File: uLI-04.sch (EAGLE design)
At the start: 40 parts, among them IC1 PIC18F14K50-I/SS, IC2 ADM2483, IC4 78L05F, J1 PICPROG2-V, J5 WEBP6-4, J6 WEBP6-4, J7 WEBP6-4, Q1 12.00 MHz, T1 IRF7306, X1 MINI-USB_SHIELD4P-USB-SPEC, X2 ARK1550/2_S

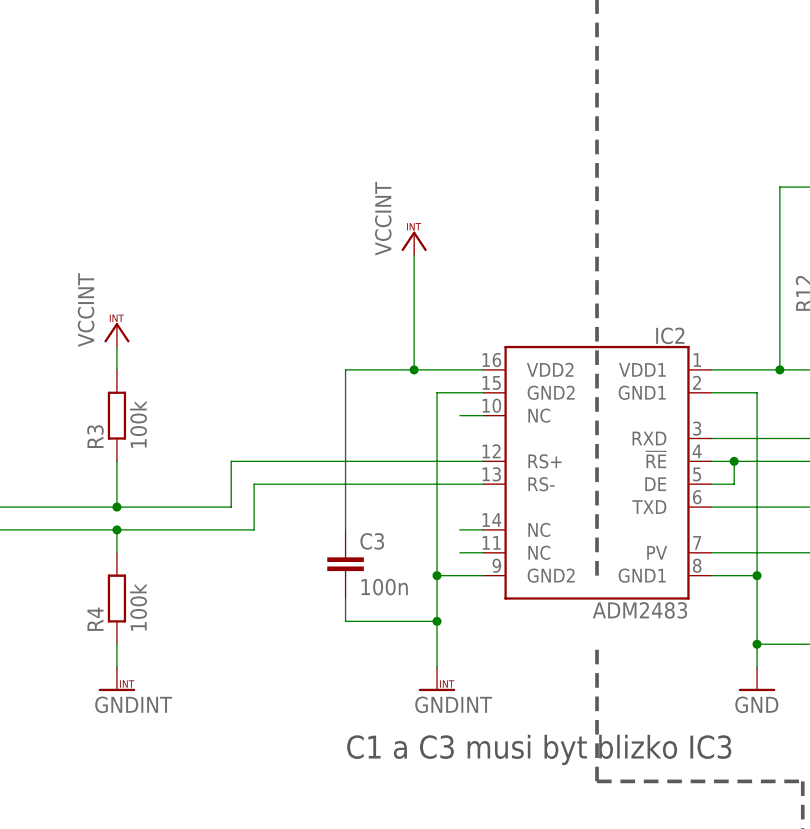
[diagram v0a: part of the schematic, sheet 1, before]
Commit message: Odstranen prebytecny kondenzator 100 n.
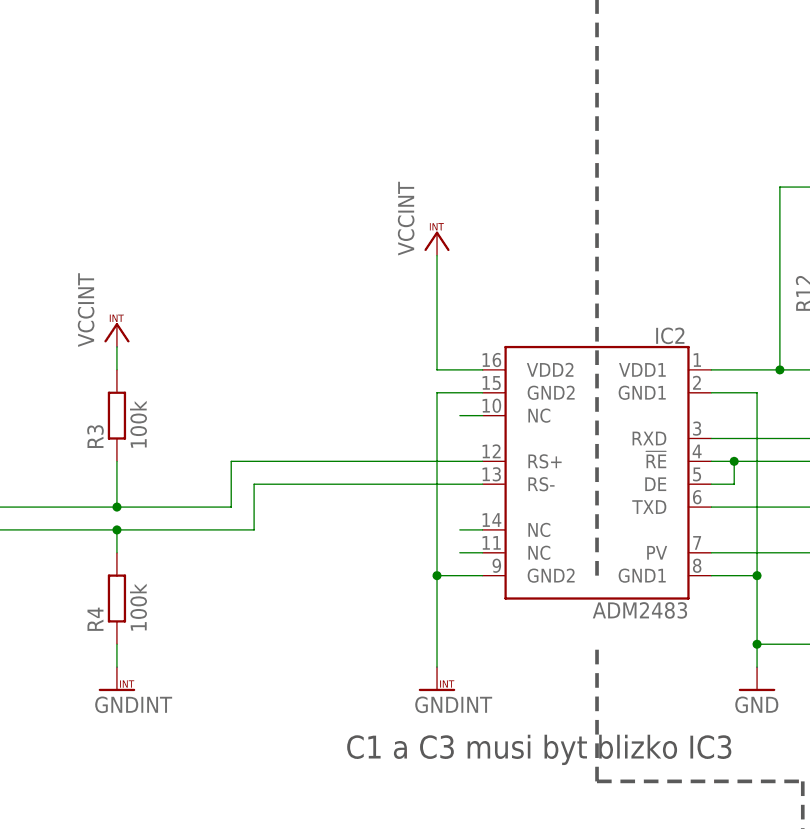
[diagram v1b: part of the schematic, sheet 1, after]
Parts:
- removed C3: 100n, rcl:C-EUC1206
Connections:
- net GNDINT: no longer C3.2
- net VCCINT: no longer C3.1
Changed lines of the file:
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@@
 </classes>
 <parts>
-<part name="C3" library="rcl" deviceset="C-EU" device="C1206" value="100n"/>
 <part name="U$1" library="frames" deviceset="FRAME_M1" device=""/>
 <part name="IC1" library="microchip" deviceset="PIC18*K50" device="-I/SS" technology="F14"/>
@@
 </plain>
 <instances>
-<instance part="C3" gate="G$1" x="91.44" y="76.2"/>
 <instance part="U$1" gate="G$1" x="0" y="0"/>
 <instance part="IC1" gate="A" x="195.58" y="91.44"/>
@@
 <instance part="GND3" gate="1" x="137.16" y="60.96"/>
 <instance part="GND4" gate="G$1" x="101.6" y="60.96"/>
-<instance part="VCC1" gate="G$1" x="99.06" y="111.76"/>
+<instance part="VCC1" gate="G$1" x="101.6" y="111.76"/>
 <instance part="C4" gate="G$1" x="147.32" y="76.2"/>
 <instance part="X1" gate="A" x="241.3" y="83.82"/>
@@
 <wire x1="101.6" y1="93.98" x2="101.6" y2="73.66" width="0.1524" layer="91"/>
 <wire x1="101.6" y1="73.66" x2="106.68" y2="73.66" width="0.1524" layer="91"/>
-<wire x1="101.6" y1="73.66" x2="101.6" y2="68.58" width="0.1524" layer="91"/>
 <junction x="101.6" y="73.66"/>
 <pinref part="GND4" gate="G$1" pin="GNDINT"/>
-<pinref part="C3" gate="G$1" pin="2"/>
-<wire x1="101.6" y1="68.58" x2="101.6" y2="63.5" width="0.1524" layer="91"/>
-<wire x1="101.6" y1="68.58" x2="91.44" y2="68.58" width="0.1524" layer="91"/>
-<wire x1="91.44" y1="68.58" x2="91.44" y2="71.12" width="0.1524" layer="91"/>
-<junction x="101.6" y="68.58"/>
+<wire x1="101.6" y1="73.66" x2="101.6" y2="63.5" width="0.1524" layer="91"/>
 <pinref part="IC2" gate="A" pin="GND2@2"/>
 <pinref part="IC2" gate="A" pin="GND2@1"/>
@@
 <net name="VCCINT" class="1">
 <segment>
-<wire x1="99.06" y1="96.52" x2="99.06" y2="109.22" width="0.1524" layer="91"/>
-<wire x1="106.68" y1="96.52" x2="99.06" y2="96.52" width="0.1524" layer="91"/>
-<junction x="99.06" y="96.52"/>
+<wire x1="101.6" y1="96.52" x2="101.6" y2="109.22" width="0.1524" layer="91"/>
+<wire x1="106.68" y1="96.52" x2="101.6" y2="96.52" width="0.1524" layer="91"/>
 <pinref part="VCC1" gate="G$1" pin="VCCINT"/>
-<pinref part="C3" gate="G$1" pin="1"/>
-<wire x1="91.44" y1="78.74" x2="91.44" y2="96.52" width="0.1524" layer="91"/>
-<wire x1="91.44" y1="96.52" x2="99.06" y2="96.52" width="0.1524" layer="91"/>
 <pinref part="IC2" gate="A" pin="VDD2"/>
 </segment>

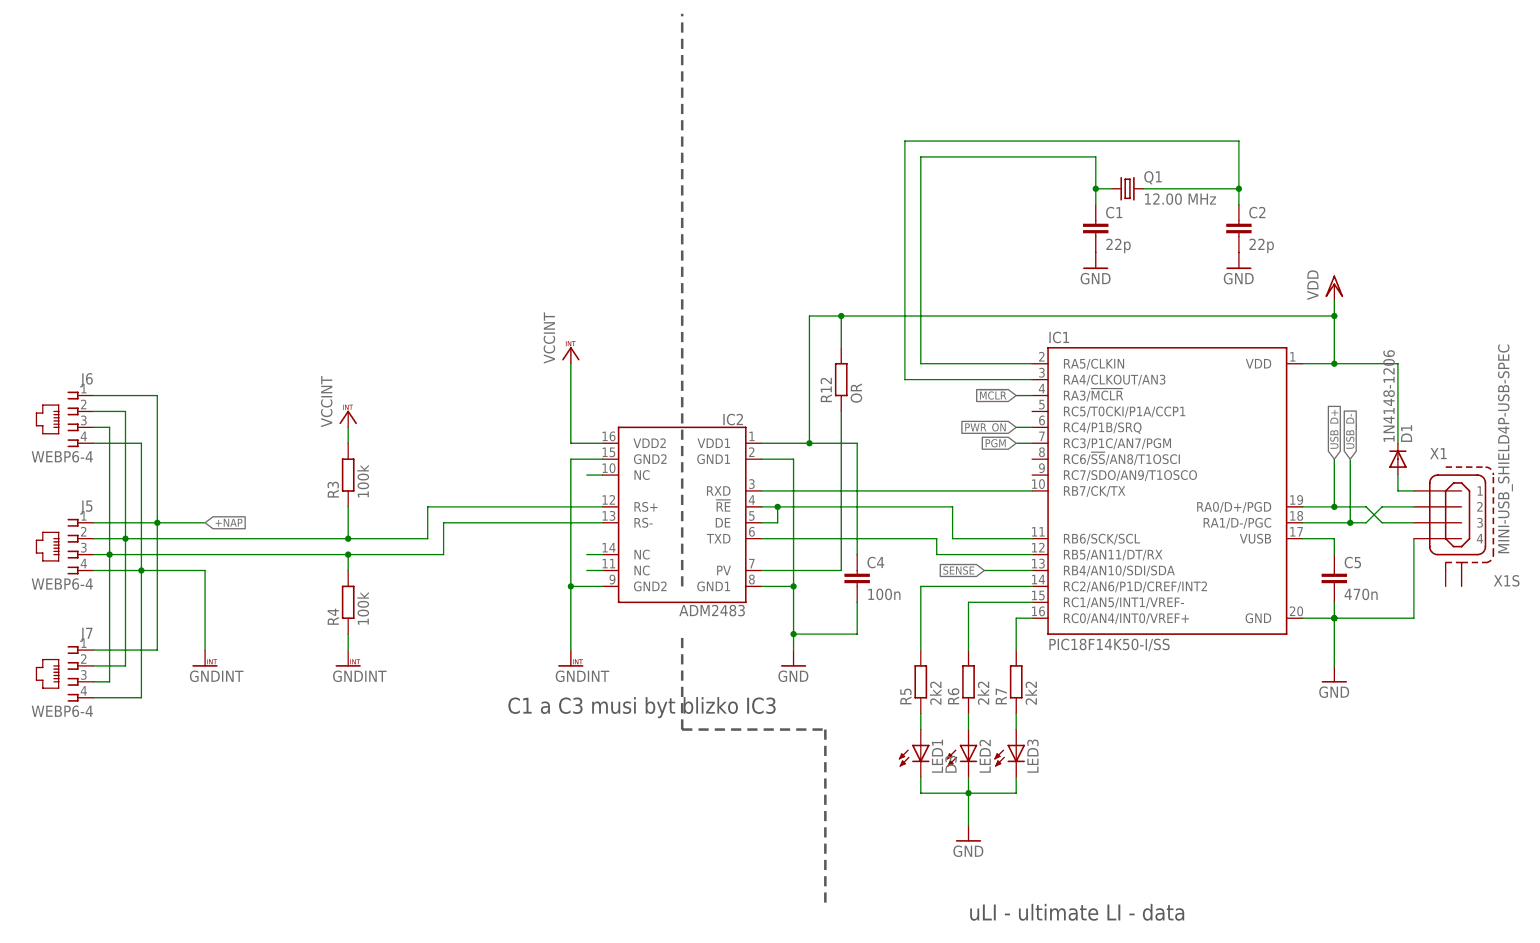
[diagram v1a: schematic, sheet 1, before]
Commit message: uLI-04 rev 2.
Opraveny chyby uLI-04 zjistene behem testovani:
 * upraven obrys krabicky podle realnych rozmeru (zvetseno symtetricky 1 mm do sirky a 0.5 mm do vysky)
 * posunuty otvory pro srouby do krabicky o 0.5 mm v kazde ose smerrem ke kraji
 * prohozeno RX a TX mezi procesorem a ADUMem
 * opraveno zdcadlove zapojeni XpressNETich konektoru
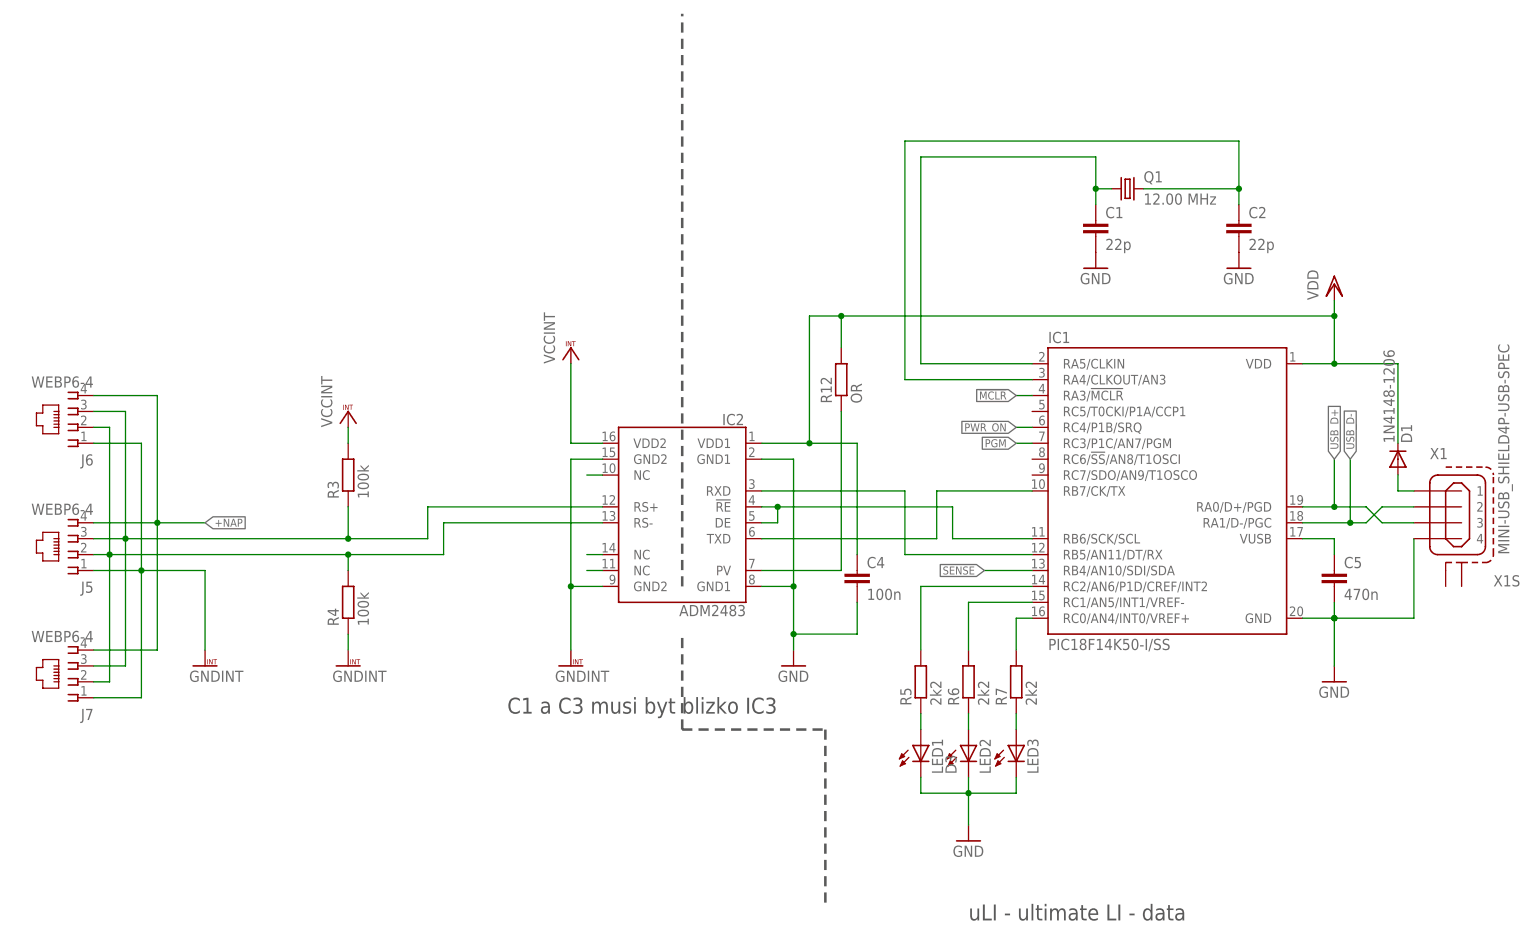
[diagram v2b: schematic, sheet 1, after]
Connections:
- removed net PROC_TX: IC1.RB7/CK/TX, IC2.RXD
- new net N$5: IC1.RB5/AN11/DT/RX, IC2.RXD
- net +NAP: now also J5.5, J6.5, J7.5; no longer J5.2, J6.2, J7.2
- net BUS_A: now also J5.4, J6.4, J7.4; no longer J5.3, J6.3, J7.3
- net BUS_B: now also J5.3, J6.3, J7.3; no longer J5.4, J6.4, J7.4
- net GNDINT: now also J5.2, J6.2, J7.2; no longer J5.5, J6.5, J7.5
- net PROC_RX: now also IC1.RB7/CK/TX; no longer IC1.RB5/AN11/DT/RX
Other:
- moved on the sheet: J5, J6, J7
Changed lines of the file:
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@@
 <instance part="GND10" gate="G$1" x="43.18" y="60.96"/>
 <instance part="IC2" gate="A" x="119.38" y="86.36" rot="MR0"/>
-<instance part="J5" gate="A" x="22.86" y="81.28" rot="MR0"/>
-<instance part="J6" gate="A" x="22.86" y="101.6" rot="MR0"/>
-<instance part="J7" gate="A" x="22.86" y="60.96" rot="MR0"/>
+<instance part="J5" gate="A" x="22.86" y="78.74" rot="R180"/>
+<instance part="J6" gate="A" x="22.86" y="99.06" rot="R180"/>
+<instance part="J7" gate="A" x="22.86" y="58.42" rot="R180"/>
 <instance part="R12" gate="G$1" x="144.78" y="106.68" rot="R90"/>
 </instances>
@@
 <net name="PROC_RX" class="0">
 <segment>
-<pinref part="IC1" gate="A" pin="RB5/AN11/DT/RX"/>
-<wire x1="175.26" y1="78.74" x2="160.02" y2="78.74" width="0.1524" layer="91"/>
 <pinref part="IC2" gate="A" pin="TXD"/>
 <wire x1="132.08" y1="81.28" x2="160.02" y2="81.28" width="0.1524" layer="91"/>
-<wire x1="160.02" y1="81.28" x2="160.02" y2="78.74" width="0.1524" layer="91"/>
-</segment>
-</net>
-<net name="PROC_TX" class="0">
-<segment>
+<wire x1="160.02" y1="81.28" x2="160.02" y2="88.9" width="0.1524" layer="91"/>
 <pinref part="IC1" gate="A" pin="RB7/CK/TX"/>
-<wire x1="175.26" y1="88.9" x2="132.08" y2="88.9" width="0.1524" layer="91"/>
-<pinref part="IC2" gate="A" pin="RXD"/>
+<wire x1="160.02" y1="88.9" x2="175.26" y2="88.9" width="0.1524" layer="91"/>
 </segment>
 </net>
@@
 </segment>
 <segment>
-<wire x1="25.4" y1="96.52" x2="33.02" y2="96.52" width="0.1524" layer="91"/>
-<wire x1="25.4" y1="76.2" x2="33.02" y2="76.2" width="0.1524" layer="91"/>
 <pinref part="GND10" gate="G$1" pin="GNDINT"/>
 <wire x1="33.02" y1="76.2" x2="43.18" y2="76.2" width="0.1524" layer="91"/>
 <wire x1="43.18" y1="76.2" x2="43.18" y2="63.5" width="0.1524" layer="91"/>
-<wire x1="25.4" y1="55.88" x2="33.02" y2="55.88" width="0.1524" layer="91"/>
 <wire x1="33.02" y1="55.88" x2="33.02" y2="76.2" width="0.1524" layer="91"/>
 <junction x="33.02" y="76.2"/>
 <wire x1="33.02" y1="96.52" x2="33.02" y2="76.2" width="0.1524" layer="91"/>
-<pinref part="J6" gate="A" pin="5"/>
-<pinref part="J5" gate="A" pin="5"/>
-<pinref part="J7" gate="A" pin="5"/>
+<pinref part="J6" gate="A" pin="2"/>
+<wire x1="25.4" y1="96.52" x2="33.02" y2="96.52" width="0.1524" layer="91"/>
+<pinref part="J7" gate="A" pin="2"/>
+<wire x1="25.4" y1="55.88" x2="33.02" y2="55.88" width="0.1524" layer="91"/>
+<pinref part="J5" gate="A" pin="2"/>
+<wire x1="25.4" y1="76.2" x2="33.02" y2="76.2" width="0.1524" layer="91"/>
 </segment>
 </net>
@@
 <pinref part="R3" gate="G$1" pin="1"/>
 <wire x1="66.04" y1="81.28" x2="30.48" y2="81.28" width="0.1524" layer="91"/>
-<wire x1="30.48" y1="81.28" x2="25.4" y2="81.28" width="0.1524" layer="91"/>
 <wire x1="66.04" y1="86.36" x2="66.04" y2="81.28" width="0.1524" layer="91"/>
 <junction x="66.04" y="81.28"/>
-<wire x1="25.4" y1="101.6" x2="30.48" y2="101.6" width="0.1524" layer="91"/>
 <wire x1="30.48" y1="101.6" x2="30.48" y2="81.28" width="0.1524" layer="91"/>
 <junction x="30.48" y="81.28"/>
@@
 <pinref part="IC2" gate="A" pin="RS+"/>
 <wire x1="66.04" y1="81.28" x2="78.74" y2="81.28" width="0.1524" layer="91"/>
+<wire x1="30.48" y1="60.96" x2="30.48" y2="81.28" width="0.1524" layer="91"/>
+<pinref part="J6" gate="A" pin="4"/>
+<wire x1="25.4" y1="101.6" x2="30.48" y2="101.6" width="0.1524" layer="91"/>
+<pinref part="J7" gate="A" pin="4"/>
 <wire x1="25.4" y1="60.96" x2="30.48" y2="60.96" width="0.1524" layer="91"/>
-<wire x1="30.48" y1="60.96" x2="30.48" y2="81.28" width="0.1524" layer="91"/>
-<pinref part="J6" gate="A" pin="3"/>
-<pinref part="J5" gate="A" pin="3"/>
-<pinref part="J7" gate="A" pin="3"/>
+<pinref part="J5" gate="A" pin="4"/>
+<wire x1="25.4" y1="81.28" x2="30.48" y2="81.28" width="0.1524" layer="91"/>
 </segment>
 </net>
@@
 <wire x1="66.04" y1="76.2" x2="66.04" y2="78.74" width="0.1524" layer="91"/>
 <junction x="66.04" y="78.74"/>
-<wire x1="25.4" y1="78.74" x2="27.94" y2="78.74" width="0.1524" layer="91"/>
 <wire x1="27.94" y1="78.74" x2="66.04" y2="78.74" width="0.1524" layer="91"/>
-<wire x1="25.4" y1="99.06" x2="27.94" y2="99.06" width="0.1524" layer="91"/>
 <wire x1="27.94" y1="99.06" x2="27.94" y2="78.74" width="0.1524" layer="91"/>
 <junction x="27.94" y="78.74"/>
@@
 <wire x1="81.28" y1="78.74" x2="81.28" y2="83.82" width="0.1524" layer="91"/>
 <wire x1="27.94" y1="78.74" x2="27.94" y2="58.42" width="0.1524" layer="91"/>
-<wire x1="27.94" y1="58.42" x2="25.4" y2="58.42" width="0.1524" layer="91"/>
-<pinref part="J6" gate="A" pin="4"/>
-<pinref part="J5" gate="A" pin="4"/>
-<pinref part="J7" gate="A" pin="4"/>
+<pinref part="J6" gate="A" pin="3"/>
+<wire x1="25.4" y1="99.06" x2="27.94" y2="99.06" width="0.1524" layer="91"/>
+<pinref part="J7" gate="A" pin="3"/>
+<wire x1="25.4" y1="58.42" x2="27.94" y2="58.42" width="0.1524" layer="91"/>
+<pinref part="J5" gate="A" pin="3"/>
+<wire x1="25.4" y1="78.74" x2="27.94" y2="78.74" width="0.1524" layer="91"/>
 </segment>
 </net>
@@
 <net name="+NAP" class="1">
 <segment>
-<wire x1="25.4" y1="83.82" x2="35.56" y2="83.82" width="0.1524" layer="91"/>
 <label x="43.18" y="83.82" size="1.27" layer="95" font="vector" ratio="12" xref="yes"/>
 <wire x1="35.56" y1="83.82" x2="43.18" y2="83.82" width="0.1524" layer="91"/>
-<wire x1="25.4" y1="104.14" x2="35.56" y2="104.14" width="0.1524" layer="91"/>
 <wire x1="35.56" y1="83.82" x2="35.56" y2="104.14" width="0.1524" layer="91"/>
 <junction x="35.56" y="83.82"/>
 <wire x1="35.56" y1="83.82" x2="35.56" y2="63.5" width="0.1524" layer="91"/>
-<wire x1="35.56" y1="63.5" x2="25.4" y2="63.5" width="0.1524" layer="91"/>
-<pinref part="J6" gate="A" pin="2"/>
-<pinref part="J5" gate="A" pin="2"/>
-<pinref part="J7" gate="A" pin="2"/>
+<pinref part="J6" gate="A" pin="5"/>
+<wire x1="35.56" y1="104.14" x2="25.4" y2="104.14" width="0.1524" layer="91"/>
+<pinref part="J7" gate="A" pin="5"/>
+<wire x1="25.4" y1="63.5" x2="35.56" y2="63.5" width="0.1524" layer="91"/>
+<pinref part="J5" gate="A" pin="5"/>
+<wire x1="25.4" y1="83.82" x2="35.56" y2="83.82" width="0.1524" layer="91"/>
 </segment>
 </net>
@@
 </segment>
 </net>
+<net name="N$5" class="0">
+<segment>
+<pinref part="IC2" gate="A" pin="RXD"/>
+<wire x1="132.08" y1="88.9" x2="154.94" y2="88.9" width="0.1524" layer="91"/>
+<wire x1="154.94" y1="88.9" x2="154.94" y2="78.74" width="0.1524" layer="91"/>
+<pinref part="IC1" gate="A" pin="RB5/AN11/DT/RX"/>
+<wire x1="154.94" y1="78.74" x2="175.26" y2="78.74" width="0.1524" layer="91"/>
+</segment>
+</net>

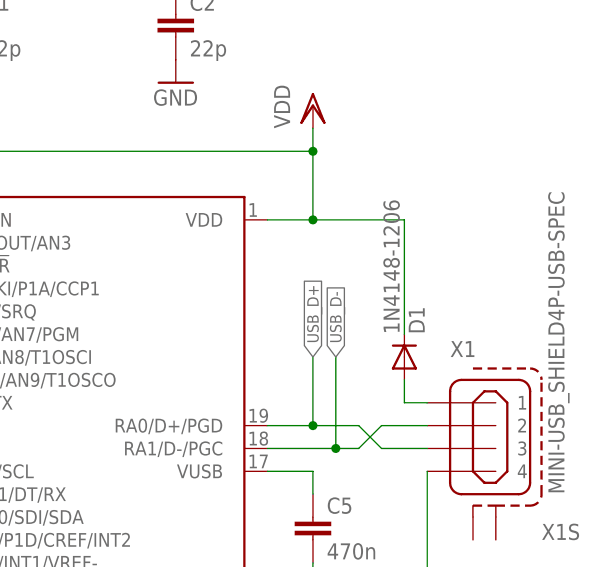
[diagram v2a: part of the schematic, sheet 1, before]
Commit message: Odstranena ochrana dioda na vstupu z USB.
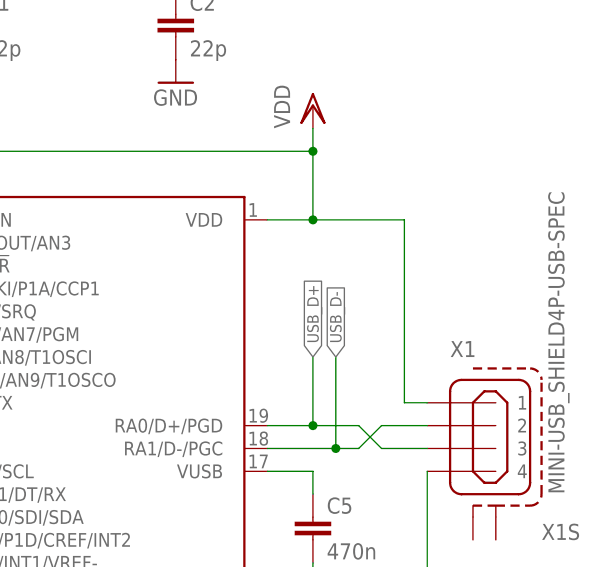
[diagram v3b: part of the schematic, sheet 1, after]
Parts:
- removed D1: 1N4148-1206, diode:1N4148-1206
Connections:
- removed net N$10: D1.A, X1A.1
- net VDD: now also X1A.1; no longer D1.C
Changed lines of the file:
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@@
 <part name="C7" library="rcl" deviceset="C-EU" device="C1206" value="100n"/>
 <part name="X1" library="con-cypressindustries" deviceset="MINI-USB_SHIELD4P-" device="USB-SPEC" value="MINI-USB_SHIELD4P-USB-SPEC"/>
-<part name="D1" library="diode" deviceset="1N4148" device="-1206"/>
 <part name="Q1" library="crystal" deviceset="XTAL" device="" value="12.00 MHz"/>
 <part name="C1" library="rcl" deviceset="C-EU" device="C0805" value="22p"/>
@@
 <instance part="X1" gate="A" x="241.3" y="83.82"/>
 <instance part="X1" gate="S" x="243.84" y="76.2"/>
-<instance part="D1" gate="A" x="233.68" y="93.98" rot="MR90"/>
 <instance part="Q1" gate="A" x="190.5" y="137.16"/>
 <instance part="C1" gate="G$1" x="185.42" y="132.08"/>
@@
 <wire x1="147.32" y1="78.74" x2="147.32" y2="96.52" width="0.1524" layer="91"/>
 <wire x1="147.32" y1="96.52" x2="139.7" y2="96.52" width="0.1524" layer="91"/>
-<pinref part="D1" gate="A" pin="C"/>
 <junction x="223.52" y="109.22"/>
 <wire x1="223.52" y1="109.22" x2="233.68" y2="109.22" width="0.1524" layer="91"/>
-<wire x1="233.68" y1="109.22" x2="233.68" y2="96.52" width="0.1524" layer="91"/>
+<wire x1="233.68" y1="109.22" x2="233.68" y2="88.9" width="0.1524" layer="91"/>
 <pinref part="IC2" gate="A" pin="VDD1"/>
 <pinref part="R12" gate="G$1" pin="2"/>
 <wire x1="144.78" y1="111.76" x2="144.78" y2="116.84" width="0.1524" layer="91"/>
 <junction x="144.78" y="116.84"/>
+<pinref part="X1" gate="A" pin="1"/>
+<wire x1="236.22" y1="88.9" x2="233.68" y2="88.9" width="0.1524" layer="91"/>
 </segment>
 </net>
@@
 </segment>
 </net>
-<net name="N$10" class="0">
-<segment>
-<pinref part="X1" gate="A" pin="1"/>
-<wire x1="236.22" y1="88.9" x2="233.68" y2="88.9" width="0.1524" layer="91"/>
-<wire x1="233.68" y1="88.9" x2="233.68" y2="91.44" width="0.1524" layer="91"/>
-<pinref part="D1" gate="A" pin="A"/>
-</segment>
-</net>
